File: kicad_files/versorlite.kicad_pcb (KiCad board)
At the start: 4 copper layers, 33 x 81.3 mm, 126 parts, among them J3 RFD900ux 10 Pin Header, J4 Conn_ARM_JTAG_SWD_10, J5 RFD900ux 3 Pin Power Select, J6 USB_C_Receptacle_USB2.0_16P, J7 Micro_SD_Card_Det2, J8 Conn_01x02_Socket, J9 IGN_1, Q1 FDMC510P-MS, Q3 AO3400A, SW1 SW_Push, SW2 SW_Push, U1 STM32F407VGTx, U10 W25Q128JVS, U11 LT1963AxST-3.3, U12 AP63205WU, U13 74LVC1G125, U2 MS5611-01BA, U3 BMI088, U4 MMC5983MA, U5 MAX-M10S, U6 BMP388, U7 LSM6DSM, U9 WE-TVS-82400102, Y1 LFXTAL036869Reel 8MHz Crystal

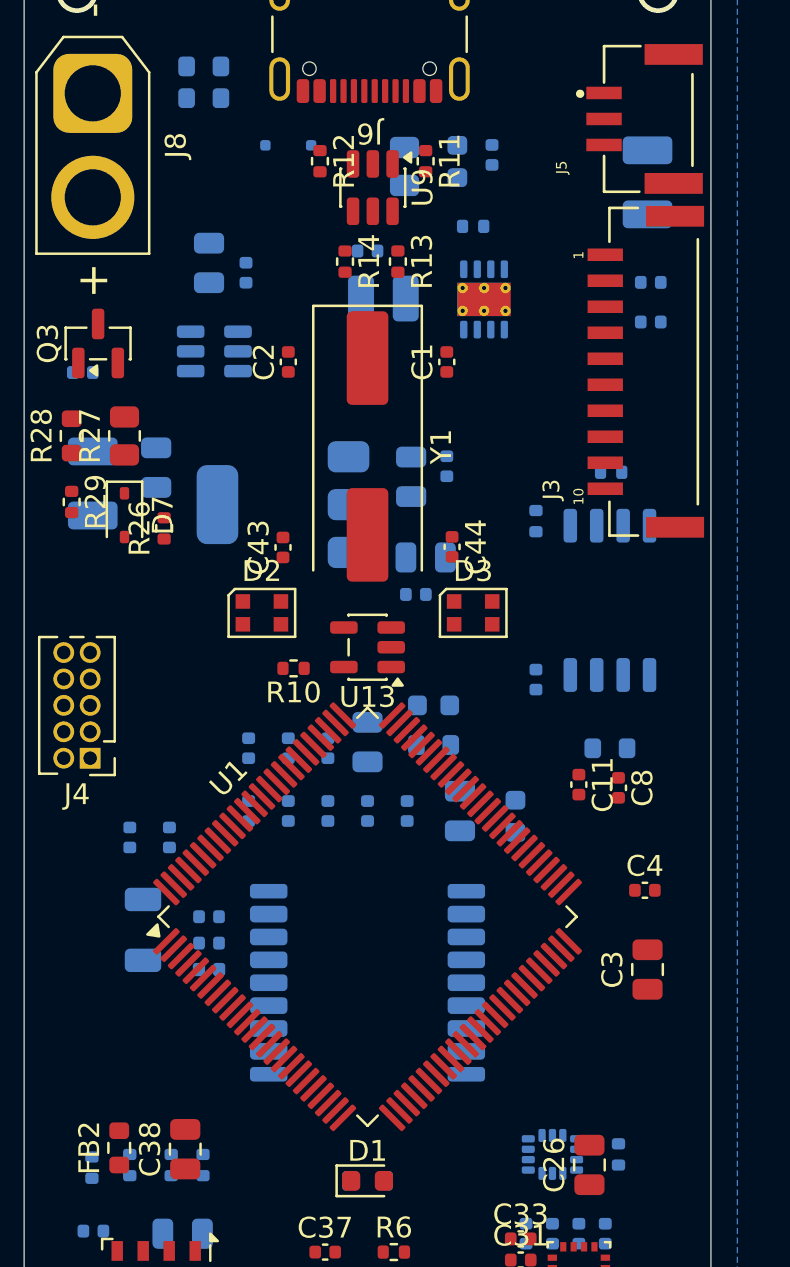
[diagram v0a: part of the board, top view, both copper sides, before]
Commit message: Improve spacing on LED and crystal
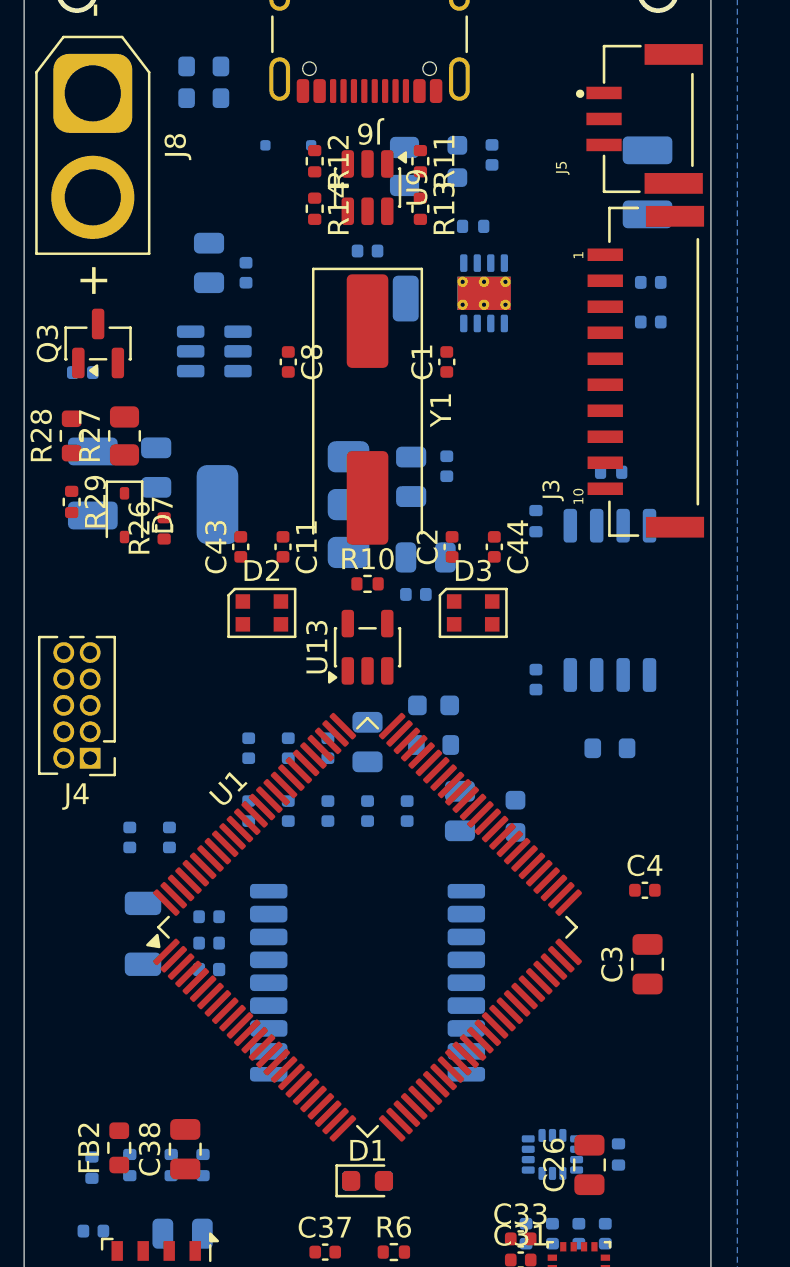
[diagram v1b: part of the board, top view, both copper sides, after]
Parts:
- moved C8 25.9 mm to (139.7, 82.5)
- moved C11 18.2 mm to (139.4, 91.4)
- moved C2 11.9 mm to (147.6, 91.4)
- moved R10 5.40 mm to (143.5, 93.2), turned to 0 degrees
- moved R14 2.93 mm to (141.0, 75.2)
- moved R13 2.76 mm to (146.1, 75.2)
- moved C43 2.03 mm to (137.4, 91.4)
- moved C44 2.03 mm to (149.6, 91.4)
- moved Y1 1.78 mm to (143.5, 84.8)
- moved U1 0.51 mm to (143.5, 109.7)
- moved Q1 0.30 mm to (149.1, 79.2)
- moved U9 0.25 mm to (143.5, 74.2)
- moved C3 0.25 mm to (157.0, 111.5)
- moved R11 0.25 mm to (146.1, 72.9)
- moved R12 0.25 mm to (141.0, 72.9)
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
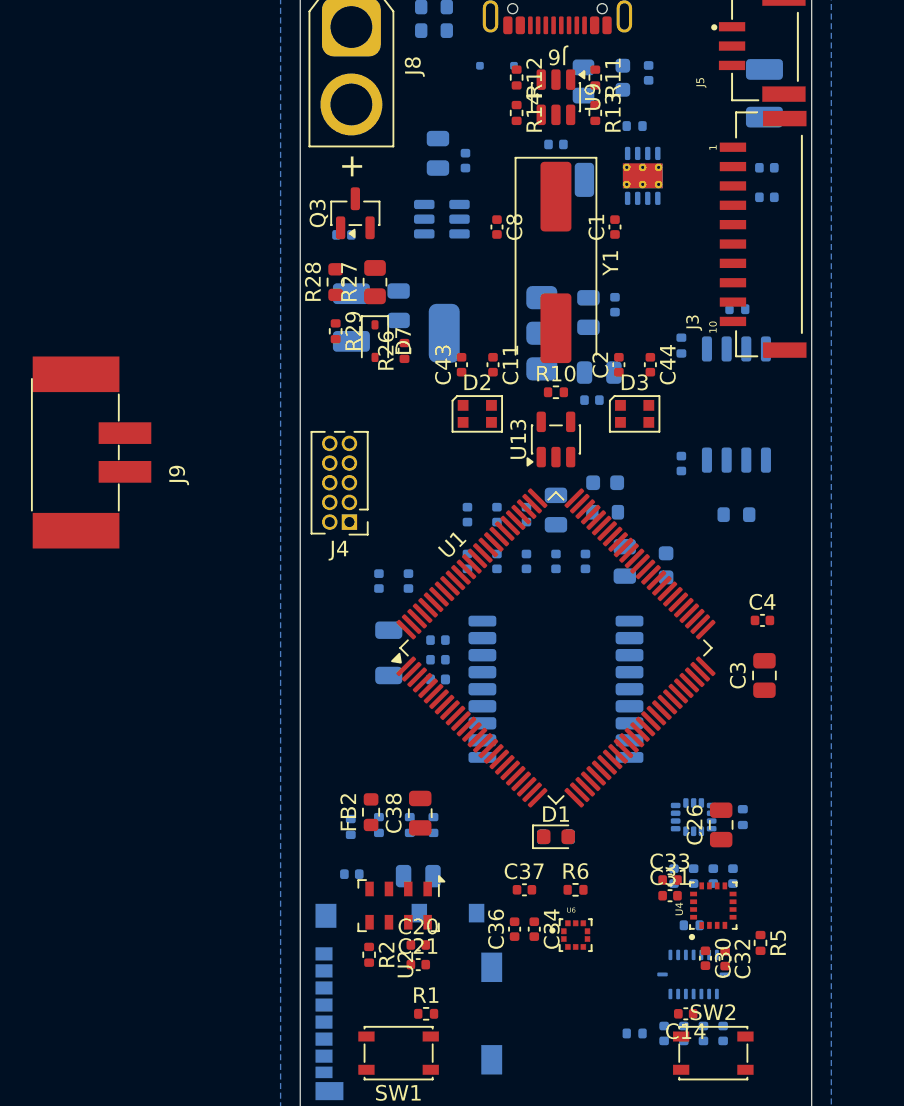
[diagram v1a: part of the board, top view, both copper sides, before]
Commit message: Sensor decoupling capacitor placement
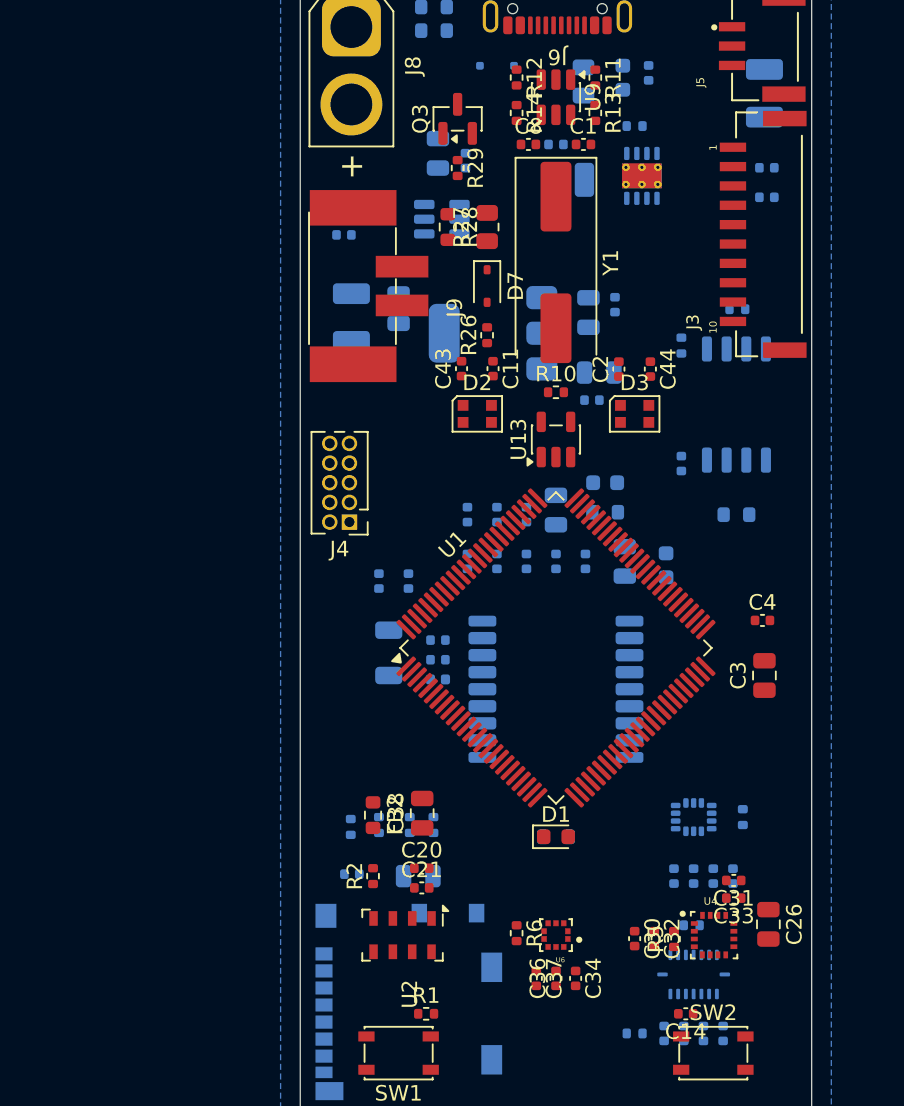
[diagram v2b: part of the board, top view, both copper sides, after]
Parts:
- moved J9 20.9 mm to (131.4, 86.4)
- moved R29 13.2 mm to (137.2, 78.7)
- moved Q3 8.99 mm to (137.2, 75.6)
- moved D7 8.07 mm to (139.1, 86.4)
- moved R27 8.07 mm to (139.1, 82.5)
- moved R28 8.07 mm to (136.5, 82.5), turned to -90 degrees
- moved C26 7.11 mm to (157.2, 127.6), turned to -90 degrees
- moved C37 5.77 mm to (142.2, 131.1), turned to -90 degrees
- moved C8 5.71 mm to (141.7, 77.2), turned to 0 degrees
- moved C1 5.71 mm to (145.3, 77.2), turned to 0 degrees
- moved R5 5.59 mm to (151.1, 128.5), turned to 90 degrees
- moved R26 5.43 mm to (139.1, 89.5)
- moved R2 5.09 mm to (131.7, 124.5), turned to 90 degrees
- moved C21 4.96 mm to (134.8, 125.2)
- moved C20 4.96 mm to (134.8, 124.0)
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
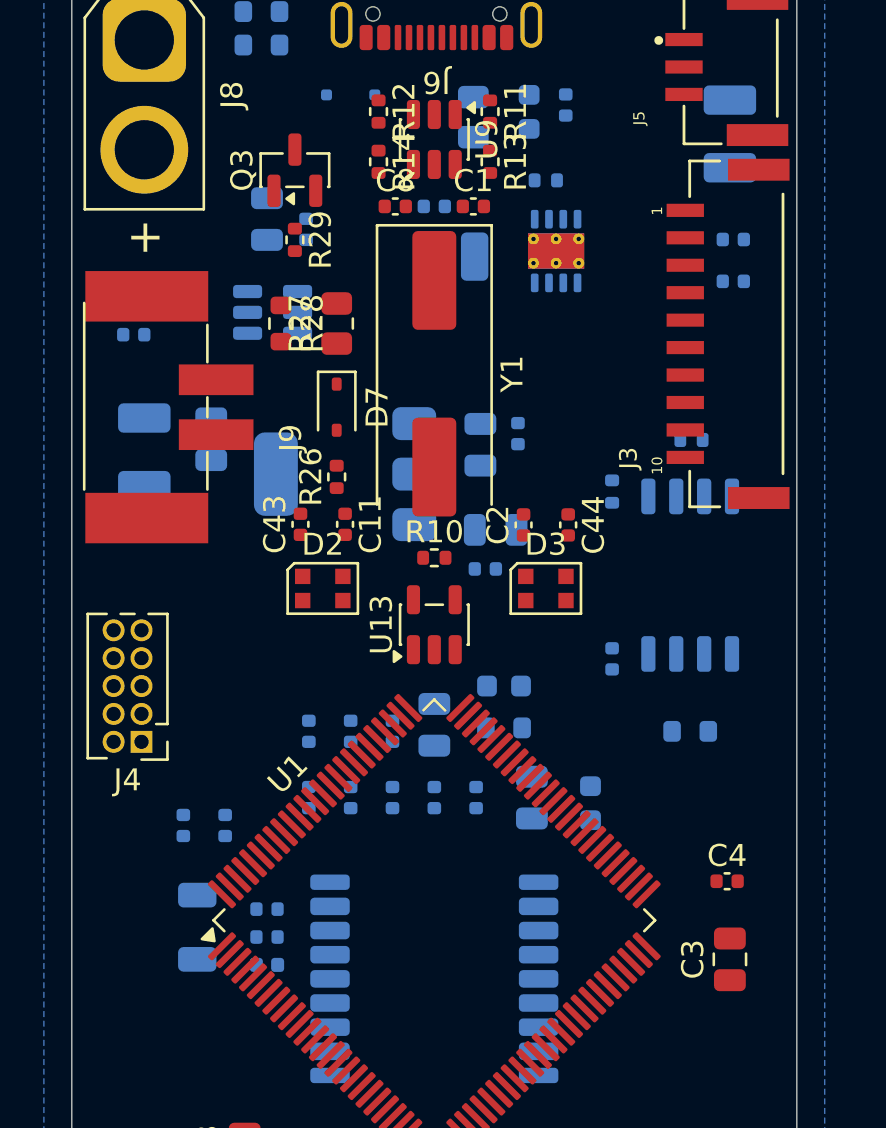
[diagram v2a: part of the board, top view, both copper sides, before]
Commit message: More component  arrangement
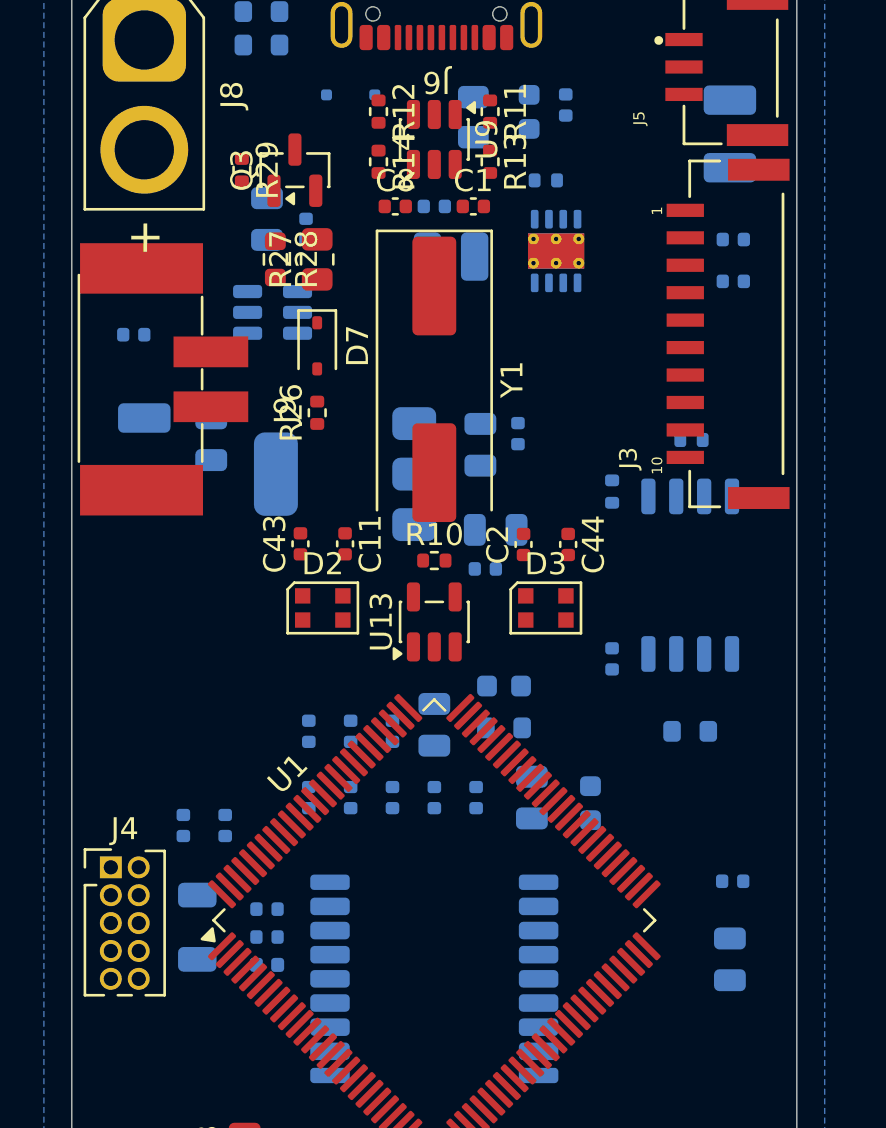
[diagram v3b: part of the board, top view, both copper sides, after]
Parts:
- C3, C4: moved to B.Cu
- moved J4 5.88 mm to (128.8, 107.3), turned to 0 degrees
- moved R29 3.99 mm to (134.7, 75.6)
- moved R26 3.05 mm to (138.2, 86.6)
- moved R27 3.05 mm to (138.2, 79.6)
- moved D7 2.93 mm to (138.2, 83.6)
- moved R28 2.93 mm to (136.3, 79.6)
- moved J9 1.29 mm to (131.2, 85.1)
- moved C2 0.89 mm to (147.6, 92.6)
- moved C44 0.89 mm to (149.6, 92.6)
- moved D2 0.89 mm to (138.4, 95.5)
- moved D3 0.89 mm to (148.6, 95.5)
- moved C11 0.89 mm to (139.4, 92.6)
- moved C43 0.89 mm to (137.4, 92.6)
- moved Y1 0.25 mm to (143.5, 85.1)
- moved C4 0.25 mm to (157.1, 108.0), turned to 180 degrees
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
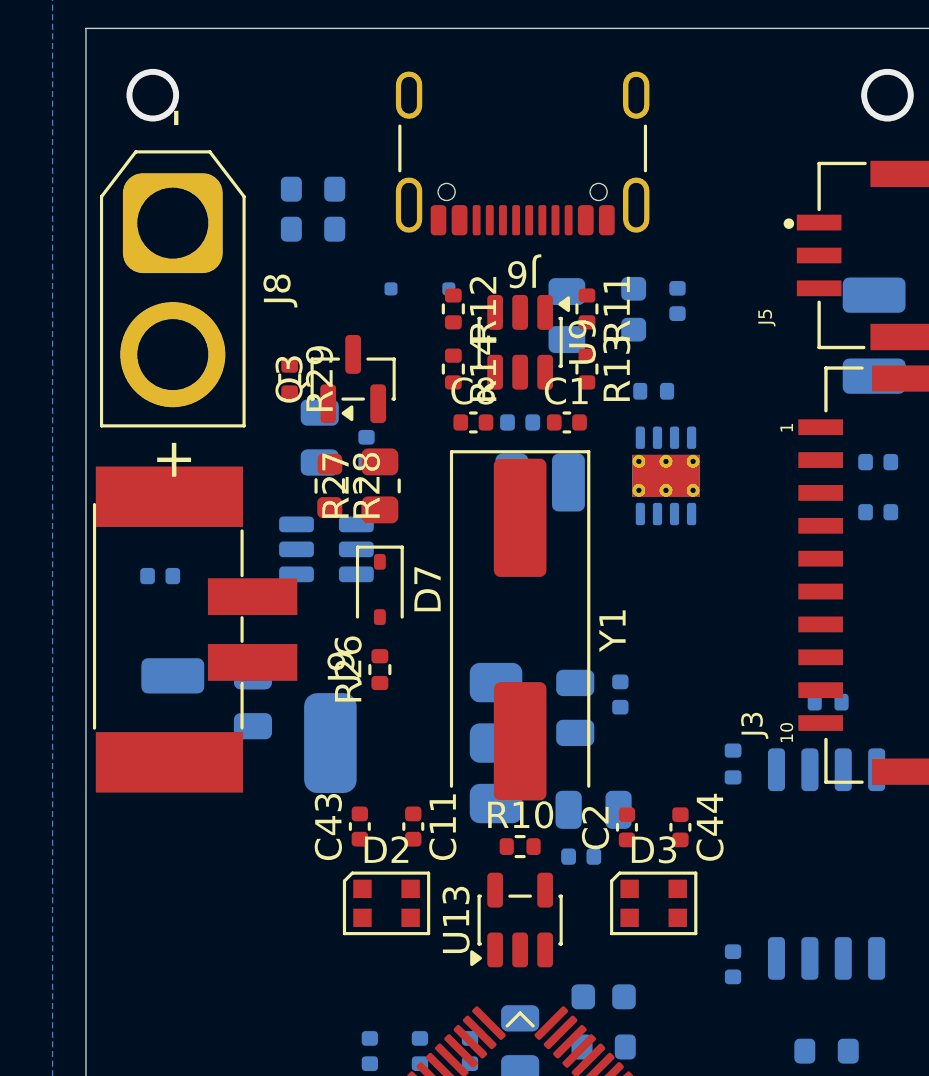
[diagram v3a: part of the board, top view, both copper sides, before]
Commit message: VBUS, BMS diodes and fuses
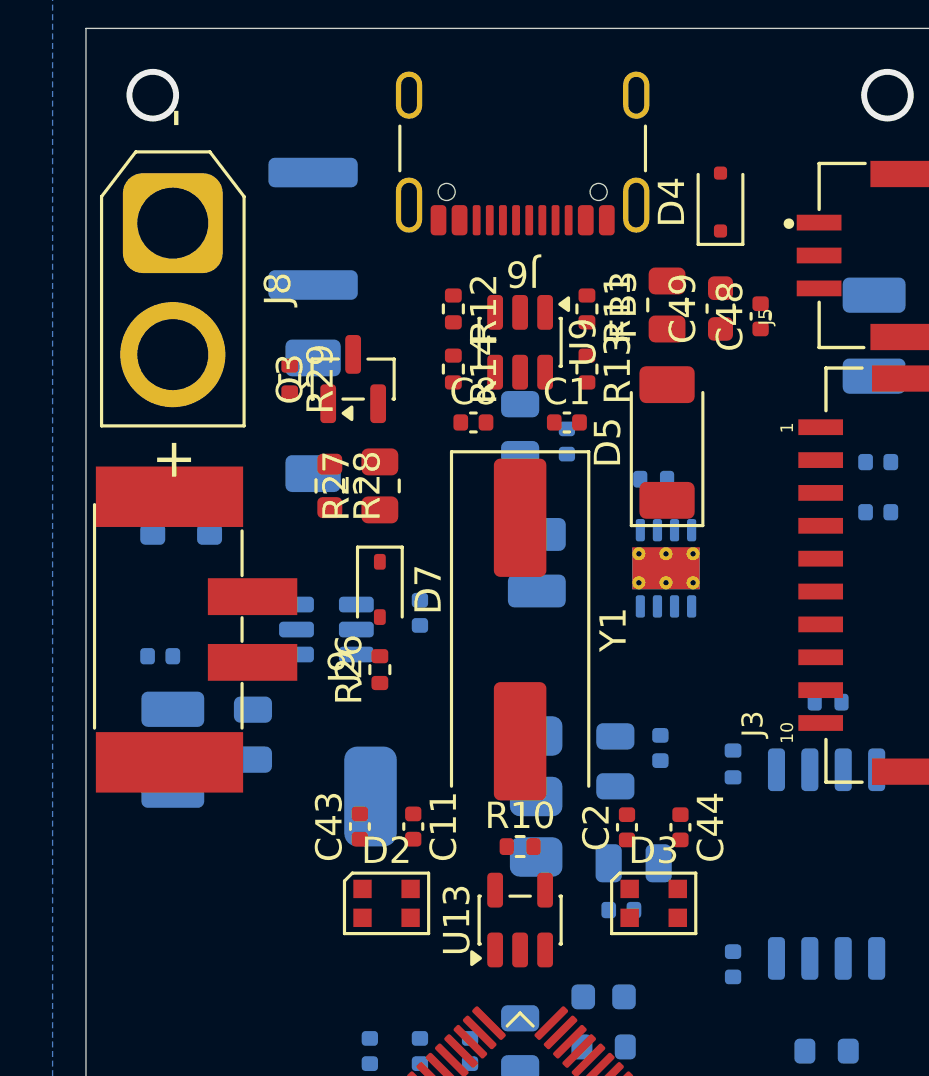
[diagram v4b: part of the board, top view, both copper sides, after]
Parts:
- added D5: PMEG6045ETPX, Diode_SMD:D_SOD-128, F.Cu at (149.1, 78.0)
- added D8: PMEG6045ETPX, Diode_SMD:D_SOD-128, B.Cu at (135.6, 77.0)
- added F1: Polyfuse, Fuse:Fuse_1812_4532Metric, B.Cu at (135.6, 69.8)
- C48, C49, D4, FB3: moved to F.Cu
- LS1: value CPT-9019S-SMT -> CMT-4023S-SMT-TR
- moved R24 12.9 mm to (131.7, 80.6), turned to -90 degrees
- moved R25 12.4 mm to (129.5, 80.6), turned to 90 degrees
- moved D4 11.9 mm to (151.1, 68.8), turned to 90 degrees
- moved C60 8.18 mm to (139.7, 84.5), turned to -90 degrees
- moved C61 7.63 mm to (145.3, 77.9)
- moved C62 7.63 mm to (143.5, 77.5)
- moved FB3 3.83 mm to (149.1, 72.7)
- moved Q1 3.51 mm to (149.1, 82.8)
- moved R22 3.34 mm to (148.6, 79.4)
- moved C49 3.30 mm to (151.1, 72.9), turned to 90 degrees
- moved C48 3.21 mm to (152.7, 73.2), turned to 90 degrees
- moved L1 3.05 mm to (144.1, 82.5), turned to 90 degrees
- moved U12 3.05 mm to (136.1, 85.1)
- moved C59 3.05 mm to (129.8, 86.1)
- moved C53 2.54 mm to (147.8, 94.0)
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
